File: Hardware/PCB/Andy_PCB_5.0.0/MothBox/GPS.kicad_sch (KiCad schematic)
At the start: 50 parts, among them U1 Days, U17 GPs 5 pin PM2.54-1*5, U2 Hours1, U6 Hours2, U7 Modes, U8 CD74HC4067M96E4, U9 CD74HC4067M96E4

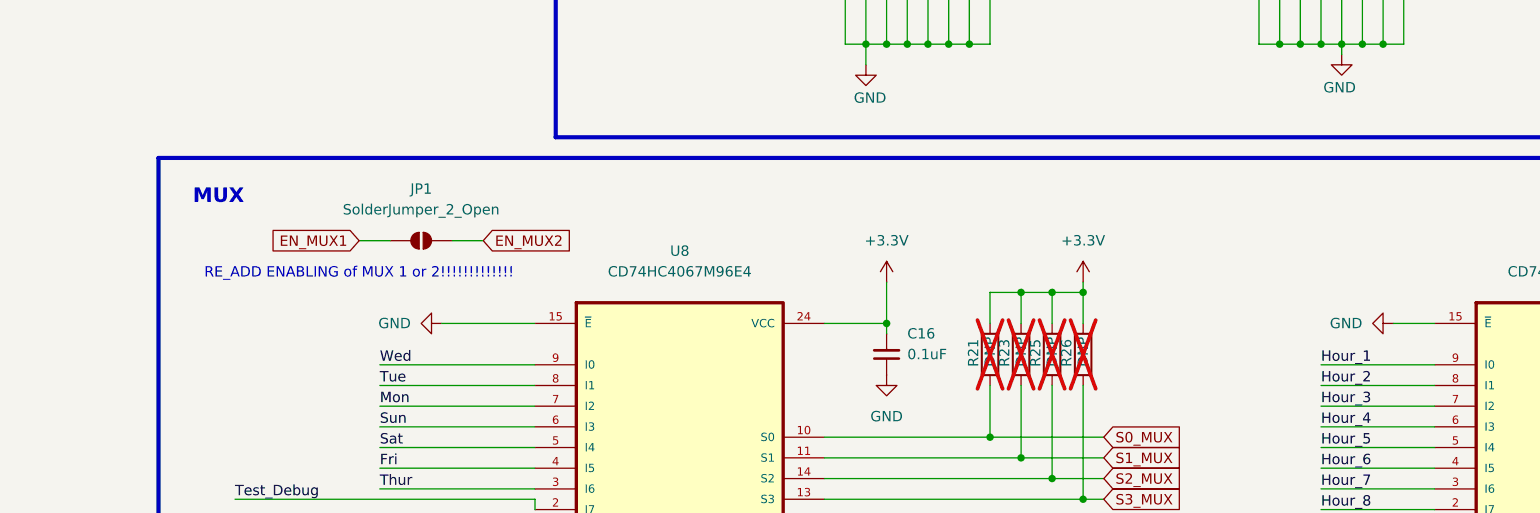
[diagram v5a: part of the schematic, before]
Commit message: Tweaked Mothbeam and added GPS footprints
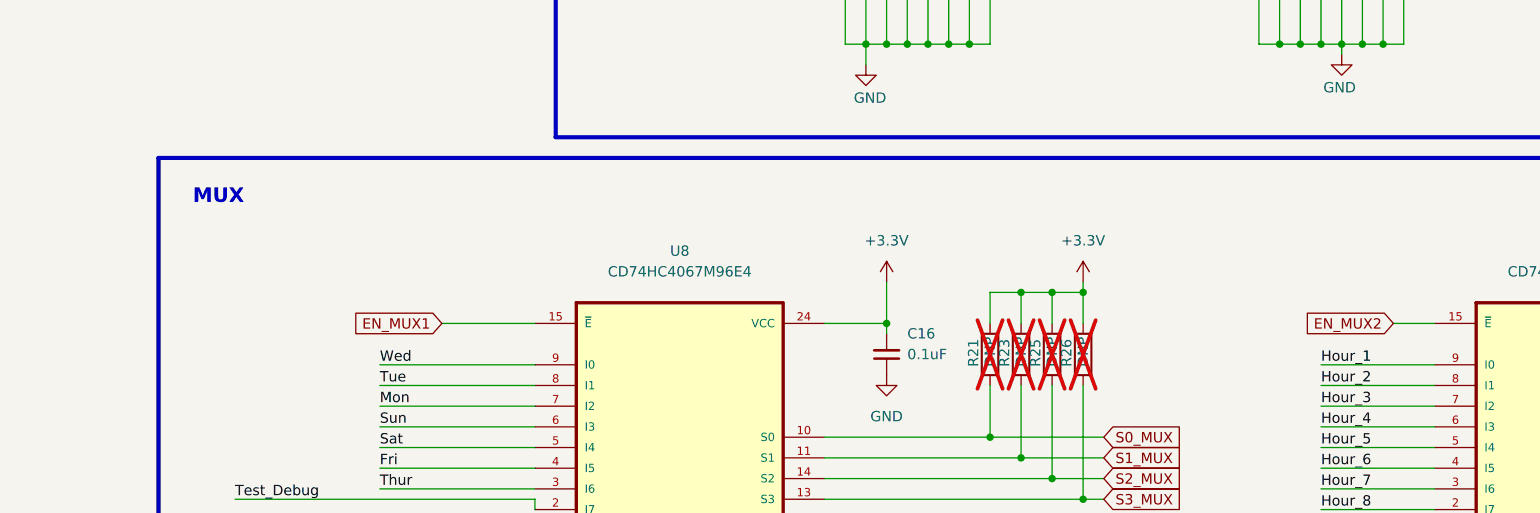
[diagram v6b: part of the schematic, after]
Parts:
- removed JP1: SolderJumper_2_Open, Jumper:SolderJumper-2_P1.3mm_Open_RoundedPad1.0x1.5mm, symbol Jumper:SolderJumper_2_Open
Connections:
- net EN_MUX1: now also U8.15 (~{E})
- net EN_MUX2: now also U9.15 (~{E})
- net GND: no longer U8.15 (~{E}), U9.15 (~{E})
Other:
- note removed: "RE_ADD ENABLING of MUX 1 or 2!!!!!!!!!!!!!"
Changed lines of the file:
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@@
 		)
 	)
-	(text "RE_ADD ENABLING of MUX 1 or 2!!!!!!!!!!!!!"
-		(exclude_from_sim no)
-		(at 60.96 123.444 0)
-		(effects
-			(font
-				(size 1.27 1.27)
-			)
-		)
-	)
 	(text "MUX\n"
 		(exclude_from_sim no)
@@
 	(wire
 		(pts
-			(xy 76.2 119.38) (xy 72.39 119.38)
-		)
-		(stroke
-			(width 0)
-			(type default)
-		)
-	)
-	(wire
-		(pts
 			(xy 195.58 54.61) (xy 186.69 54.61)
 		)
@@
 	(wire
 		(pts
-			(xy 60.96 119.38) (xy 64.77 119.38)
-		)
-		(stroke
-			(width 0)
-			(type default)
-		)
-	)
-	(wire
-		(pts
 			(xy 181.61 95.25) (xy 181.61 96.52)
 		)
@@
 		)
 	)
-	(global_label "GPS_PPS"
+	(global_label "EN_MUX2"
 		(shape input)
-		(at 33.02 74.93 180)
+		(at 187.96 129.54 180)
 		(fields_autoplaced yes)
 		(effects
@@
 		)
 		(property "Intersheetrefs" "${INTERSHEET_REFS}"
-			(at 21.5682 74.93 0)
+			(at 176.3268 129.54 0)
 			(effects
 				(font
@@
 		)
 	)
-	(global_label "EN_MUX1"
+	(global_label "GPS_PPS"
 		(shape input)
-		(at 60.96 119.38 180)
+		(at 33.02 74.93 180)
 		(fields_autoplaced yes)
 		(effects
@@
 		)
 		(property "Intersheetrefs" "${INTERSHEET_REFS}"
-			(at 49.3268 119.38 0)
+			(at 21.5682 74.93 0)
 			(effects
 				(font
@@
 		)
 	)
+	(global_label "EN_MUX1"
+		(shape input)
+		(at 71.12 129.54 180)
+		(fields_autoplaced yes)
+		(effects
+			(font
+				(size 1.27 1.27)
+			)
+			(justify right)
+		)
+		(property "Intersheetrefs" "${INTERSHEET_REFS}"
+			(at 59.4868 129.54 0)
+			(effects
+				(font
+					(size 1.27 1.27)
+				)
+				(justify right)
+				(hide yes)
+			)
+		)
+	)
 	(global_label "COM_I{slash}O"
 		(shape input)
@@
 		)
 	)
-	(global_label "EN_MUX2"
-		(shape input)
-		(at 76.2 119.38 0)
-		(fields_autoplaced yes)
-		(effects
-			(font
-				(size 1.27 1.27)
-			)
-			(justify left)
-		)
-		(property "Intersheetrefs" "${INTERSHEET_REFS}"
-			(at 87.8332 119.38 0)
-			(effects
-				(font
-					(size 1.27 1.27)
-				)
-				(justify left)
-				(hide yes)
-			)
-		)
-	)
 	(symbol
 		(lib_id "power:+3.3V")
@@
 	)
 	(symbol
-		(lib_id "Jumper:SolderJumper_2_Open")
-		(at 68.58 119.38 0)
-		(unit 1)
-		(exclude_from_sim no)
-		(in_bom no)
-		(on_board yes)
-		(dnp no)
-		(fields_autoplaced yes)
-		(property "Reference" "JP1"
-			(at 68.58 113.03 0)
-			(effects
-				(font
-					(size 1.27 1.27)
-				)
-			)
-		)
-		(property "Value" "SolderJumper_2_Open"
-			(at 68.58 115.57 0)
-			(effects
-				(font
-					(size 1.27 1.27)
-				)
-			)
-		)
-		(property "Footprint" "Jumper:SolderJumper-2_P1.3mm_Open_RoundedPad1.0x1.5mm"
-			(at 68.58 119.38 0)
-			(effects
-				(font
-					(size 1.27 1.27)
-				)
-				(hide yes)
-			)
-		)
-		(property "Datasheet" "~"
-			(at 68.58 119.38 0)
-			(effects
-				(font
-					(size 1.27 1.27)
-				)
-				(hide yes)
-			)
-		)
-		(property "Description" "Solder Jumper, 2-pole, open"
-			(at 68.58 119.38 0)
-			(effects
-				(font
-					(size 1.27 1.27)
-				)
-				(hide yes)
-			)
-		)
-		(property "LCSC PN" ""
-			(at 68.58 119.38 0)
-			(effects
-				(font
-					(size 1.27 1.27)
-				)
-			)
-		)
-		(pin "1"
-		)
-		(pin "2"
-		)
-		(instances
-			(project ""
-				(path "/9021e528-fc76-4423-a3f3-30f5652071cc/d22974ea-9095-4b9a-829f-a5d553626ed9"
-					(reference "JP1")
-					(unit 1)
-				)
-			)
-		)
-	)
-	(symbol
 		(lib_id "Device:R")
 		(at 265.43 43.18 0)
@@
 	)
 	(symbol
-		(lib_id "power:GND")
-		(at 71.12 129.54 270)
-		(unit 1)
-		(exclude_from_sim no)
-		(in_bom yes)
-		(on_board yes)
-		(dnp no)
-		(fields_autoplaced yes)
-		(property "Reference" "#PWR05"
-			(at 64.77 129.54 0)
-			(effects
-				(font
-					(size 1.27 1.27)
-				)
-				(hide yes)
-			)
-		)
-		(property "Value" "GND"
-			(at 67.31 129.5399 90)
-			(effects
-				(font
-					(size 1.27 1.27)
-				)
-				(justify right)
-			)
-		)
-		(property "Footprint" ""
-			(at 71.12 129.54 0)
-			(effects
-				(font
-					(size 1.27 1.27)
-				)
-				(hide yes)
-			)
-		)
-		(property "Datasheet" ""
-			(at 71.12 129.54 0)
-			(effects
-				(font
-					(size 1.27 1.27)
-				)
-				(hide yes)
-			)
-		)
-		(property "Description" "Power symbol creates a global label with name \"GND\" , ground"
-			(at 71.12 129.54 0)
-			(effects
-				(font
-					(size 1.27 1.27)
-				)
-				(hide yes)
-			)
-		)
-		(pin "1"
-		)
-		(instances
-			(project "MothBox"
-				(path "/9021e528-fc76-4423-a3f3-30f5652071cc/d22974ea-9095-4b9a-829f-a5d553626ed9"
-					(reference "#PWR05")
-					(unit 1)
-				)
-			)
-		)
-	)
-	(symbol
 		(lib_id "Device:R")
 		(at 156.21 45.72 0)
@@
 					(unit 1)
 				)
-			)
-		)
-	)
-	(symbol
-		(lib_id "power:GND")
-		(at 187.96 129.54 270)
-		(unit 1)
-		(exclude_from_sim no)
-		(in_bom yes)
-		(on_board yes)
-		(dnp no)
-		(fields_autoplaced yes)
-		(property "Reference" "#PWR08"
-			(at 181.61 129.54 0)
-			(effects
-				(font
-					(size 1.27 1.27)
-				)
-				(hide yes)
-			)
-		)
-		(property "Value" "GND"
-			(at 184.15 129.5399 90)
-			(effects
-				(font
-					(size 1.27 1.27)
-				)
-				(justify right)
-			)
-		)
-		(property "Footprint" ""
-			(at 187.96 129.54 0)
-			(effects
-				(font
-					(size 1.27 1.27)
-				)
-				(hide yes)
-			)
-		)
-		(property "Datasheet" ""
-			(at 187.96 129.54 0)
-			(effects
-				(font
-					(size 1.27 1.27)
-				)
-				(hide yes)
-			)
-		)
-		(property "Description" "Power symbol creates a global label with name \"GND\" , ground"
-			(at 187.96 129.54 0)
-			(effects
-				(font
-					(size 1.27 1.27)
-				)
-				(hide yes)
-			)
-		)
-		(pin "1"
-		)
-		(instances
-			(project "MothBox"
-				(path "/9021e528-fc76-4423-a3f3-30f5652071cc/d22974ea-9095-4b9a-829f-a5d553626ed9"
-					(reference "#PWR08")
-					(unit 1)
-				)

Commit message: before i kill the pullup resistors
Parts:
- removed R21, R23, R25, R26, R39, R42, R43, R44: DNP, Resistor_SMD:R_0805_2012Metric, symbol Device:R
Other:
- note removed: "CHeck datasheet for setting up this logic"

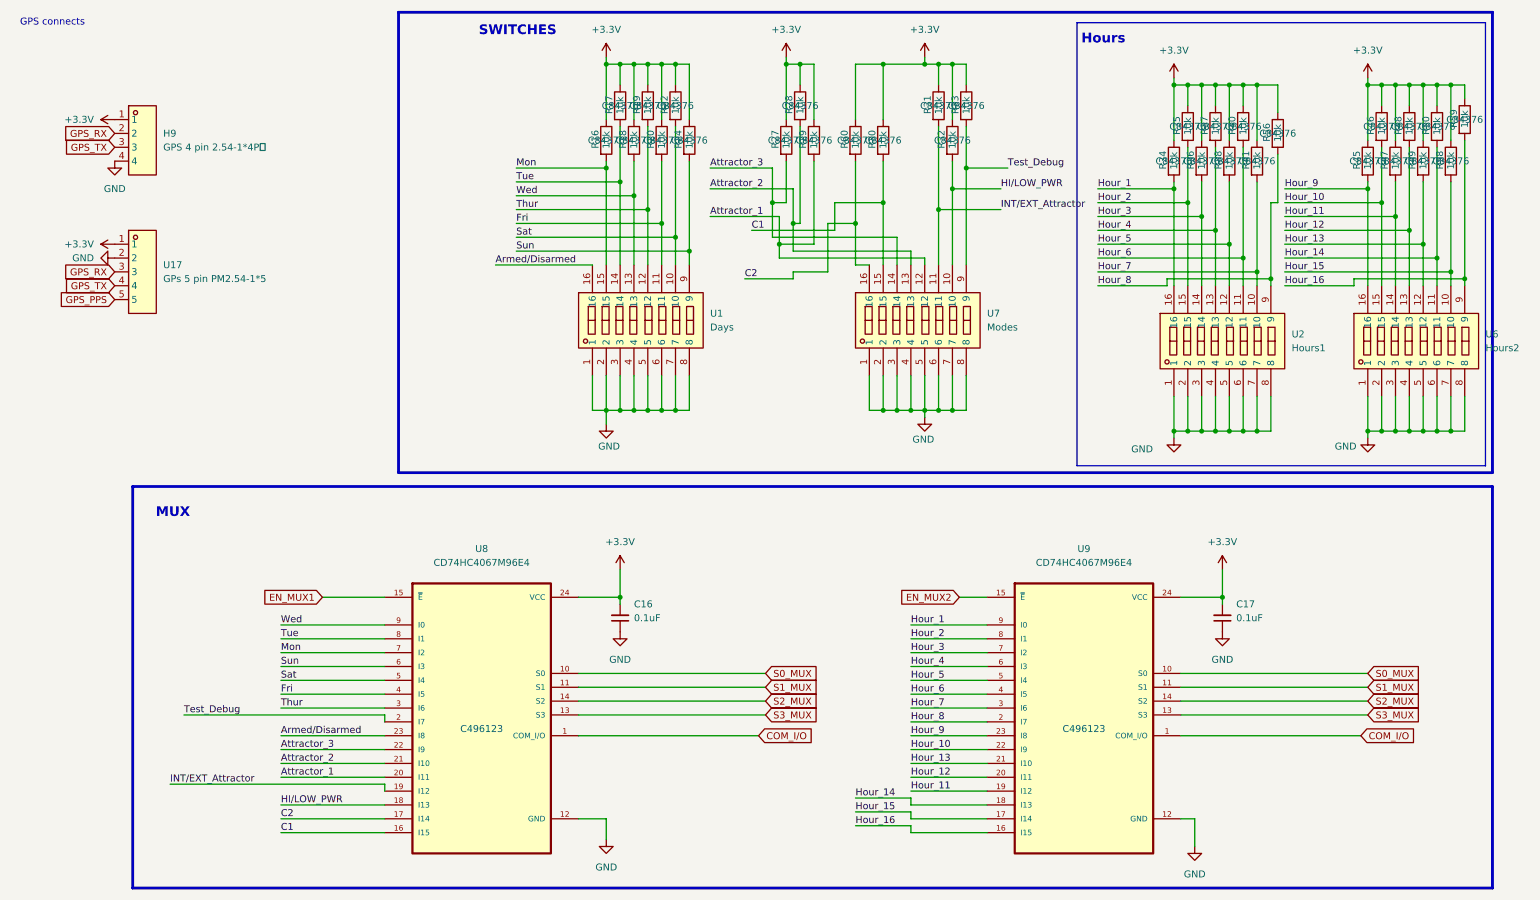
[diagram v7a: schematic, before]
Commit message: Groups photos leds, started routing
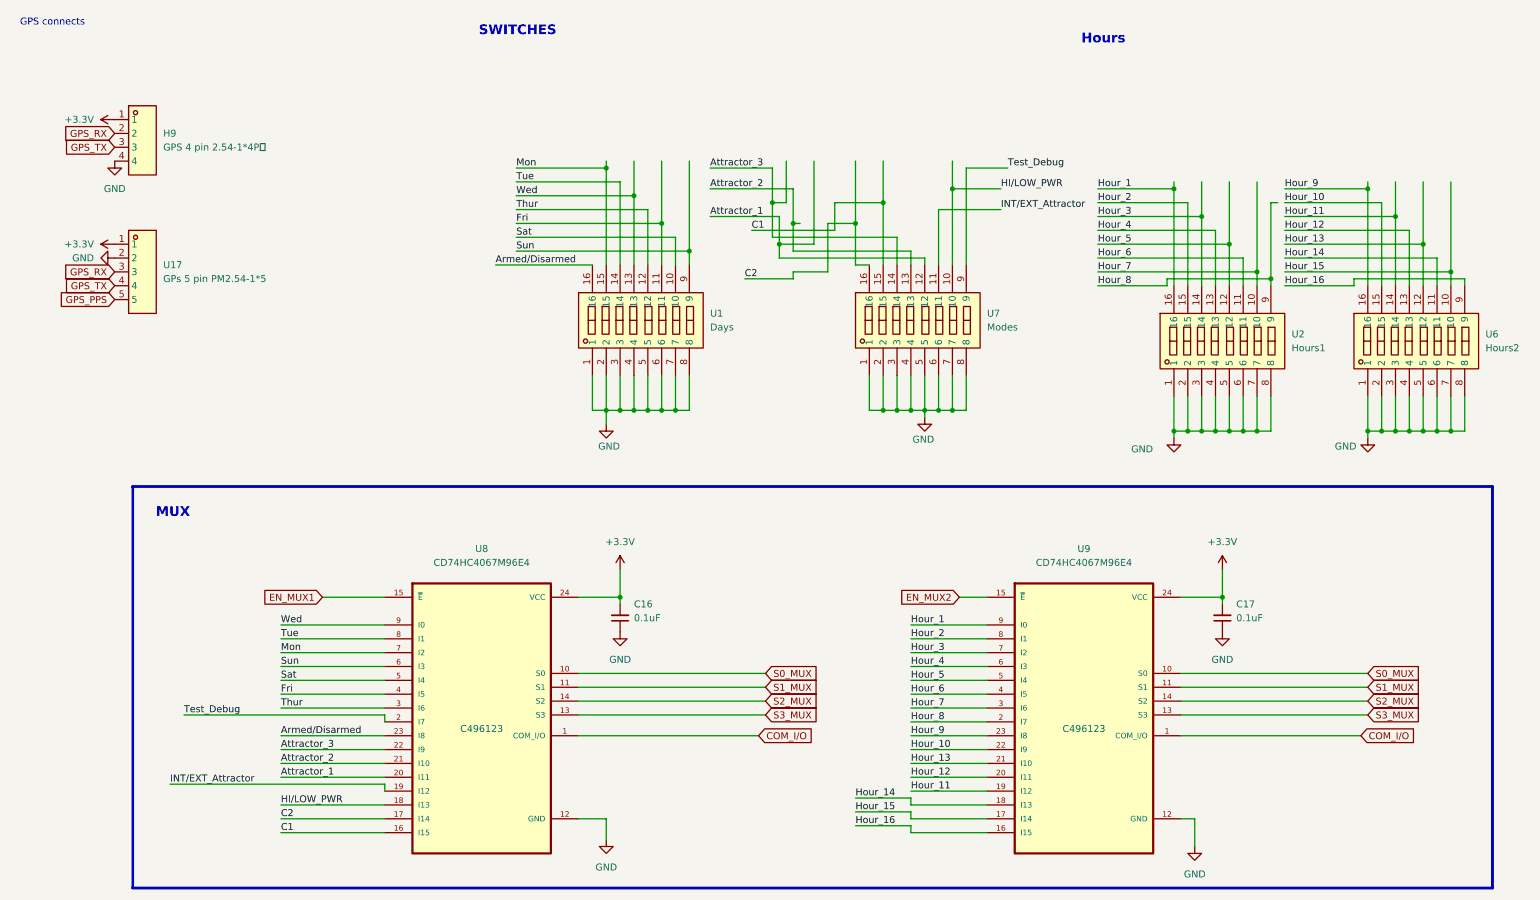
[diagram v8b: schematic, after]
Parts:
- removed R16, R17, R18, R19, R20, R22, R24, R27, R28, R29, R30, R31, R32, R33, R34, R35, R36, R37, R38, R40, R41, R45, R46, R47, R48, R49, R50, R56, R58, R59, R60: 10k, Resistor_SMD:R_0805_2012Metric, symbol Device:R
